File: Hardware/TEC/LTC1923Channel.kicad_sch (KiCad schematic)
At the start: 65 parts, among them J3 Conn_01x04, Q3 2N7002PW, Q4 2N7002PW, Q5 2N7002PW, Q6 2N7002PW, Q7 SQJ504EP, Q8 SQJ504EP, U4 LTC2053, U5 LTC1923EUH, U6 LTC1693-1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

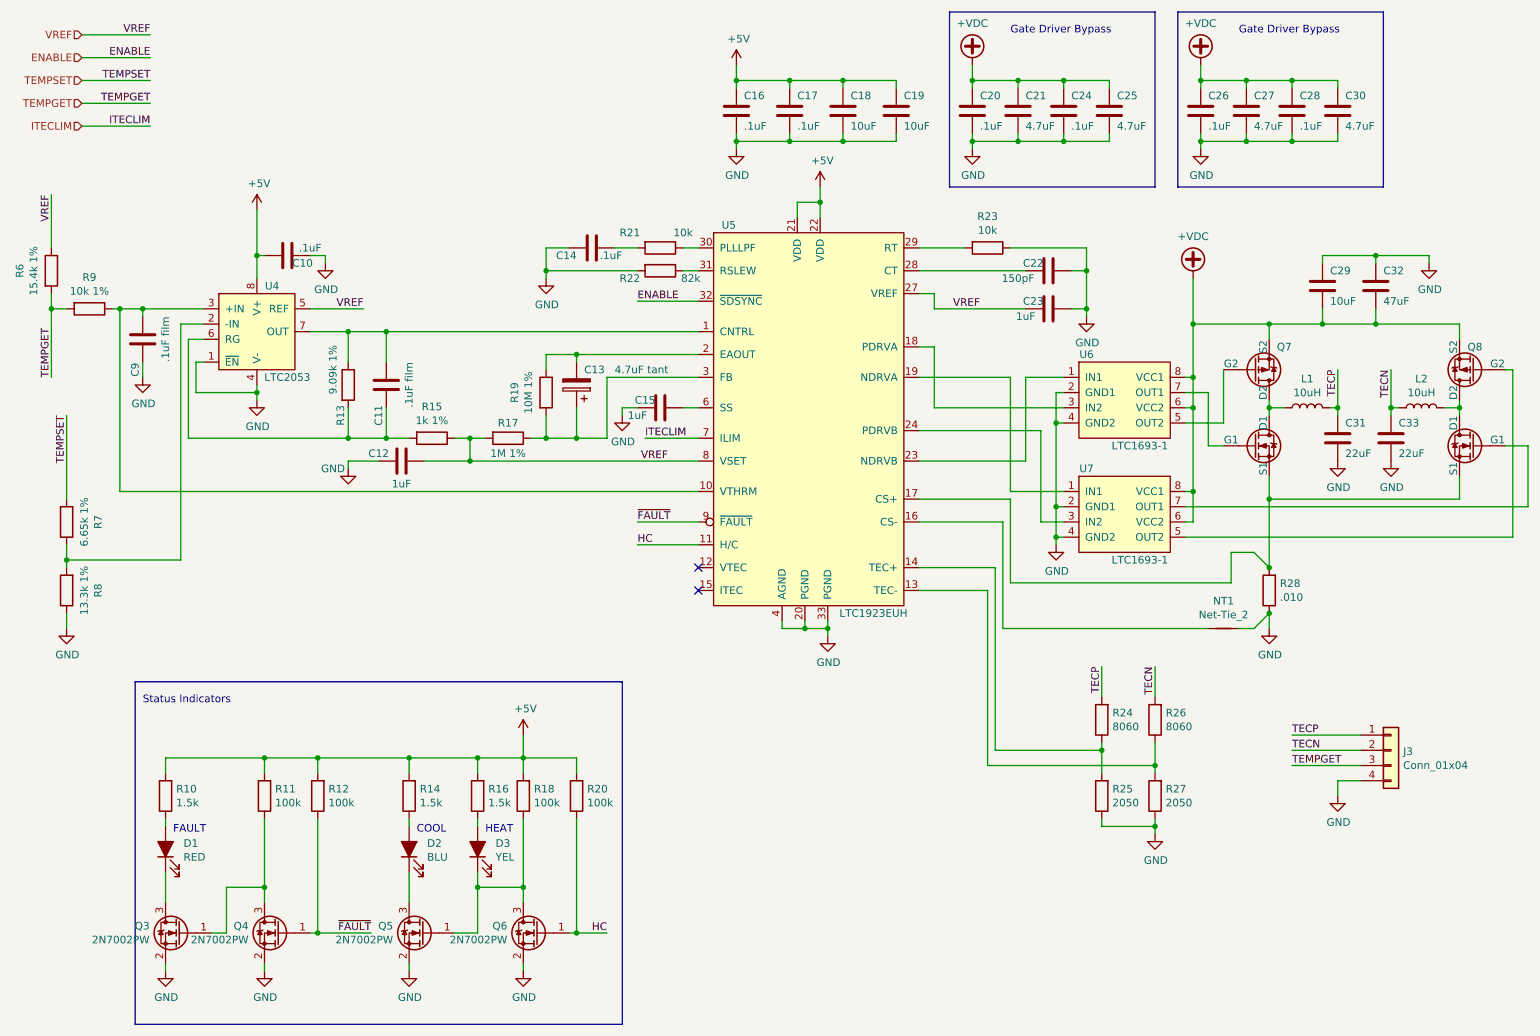
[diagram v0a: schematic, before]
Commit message: Update to kicad 8
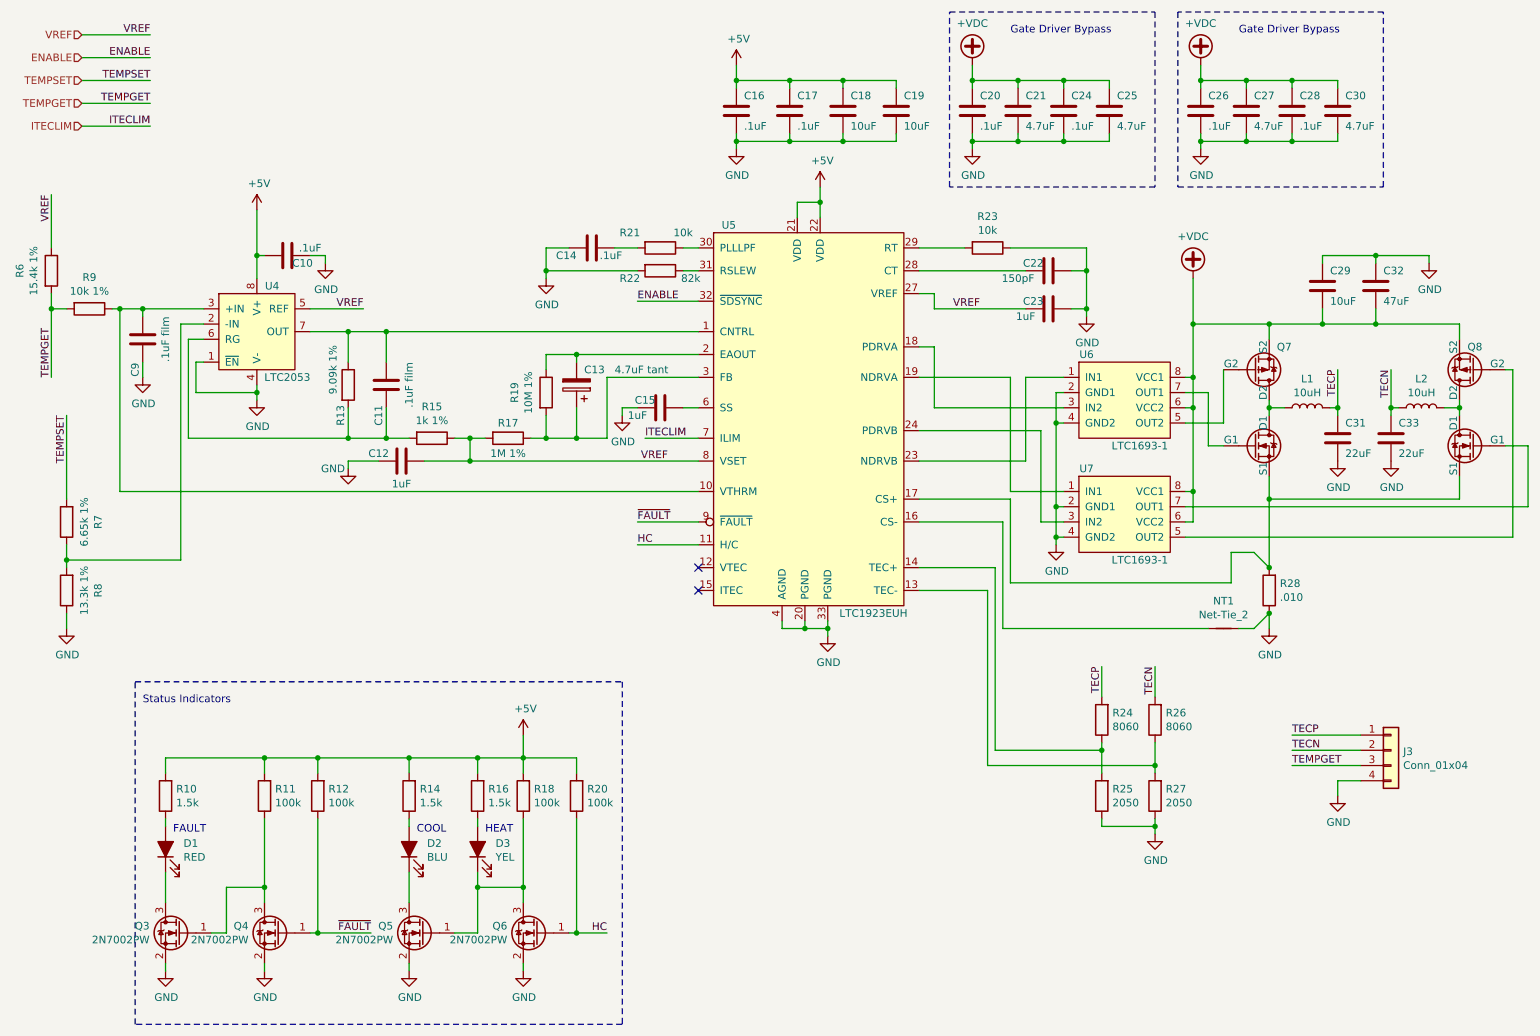
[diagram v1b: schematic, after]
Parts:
- NT1: now left out of the parts list
- Q3, Q4, Q5, Q6: footprint Package_TO_SOT_SMD:SOT-323_SC-70 -> Package_TO_SOT_SMD:SOT-23
